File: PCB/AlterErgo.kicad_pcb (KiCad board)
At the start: 2 copper layers, 104 parts, among them J1 GS3, J2 SJ-43514, J3 GS3, J4 Conn_01x02, SW0:10 SW_Push, SW0:11 SW_Push, SW0:12 SW_Push, SW0:7 SW_Push, SW0:8 SW_Push, SW0:9 SW_Push, SW1 SW_SPST, SW1:10 SW_Push, SW1:11 SW_Push, SW1:12 SW_Push, SW1:13 SW_Push, SW1:7 SW_Push, SW1:8 SW_Push, SW1:9 SW_Push, SW2:10 SW_Push, SW2:11 SW_Push, SW2:12 SW_Push, SW2:13 SW_Push, SW2:7 SW_Push, SW2:8 SW_Push, SW2:9 SW_Push, SW3:10 SW_Push, SW3:11 SW_Push, SW3:12 SW_Push, SW3:13 SW_Push, SW3:8 SW_Push, SW3:9 SW_Push, SW4:10 SW_Push, SW4:11 SW_Push, SW4:12 SW_Push, SW4:13 SW_Push, SW4:7 SW_Push, SW4:8 SW_Push, SW4:9 SW_Push, SW5:10 SW_Push, SW5:11 SW_Push, SW5:12 SW_Push, SW5:13 SW_Push, SW5:7 SW_Push, SW5:8 SW_Push, SW5:9 SW_Push, U1 Feather32u4Bluefruit, U2 MCP23018

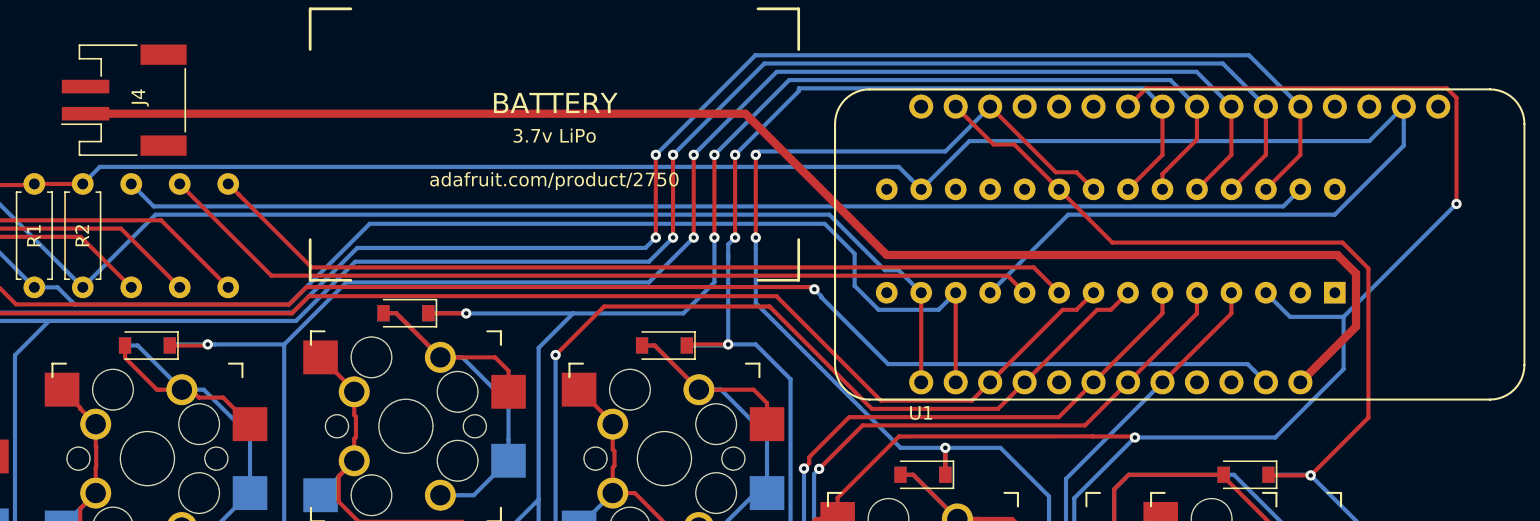
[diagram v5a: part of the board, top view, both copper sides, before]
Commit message: Fix some DRC errors
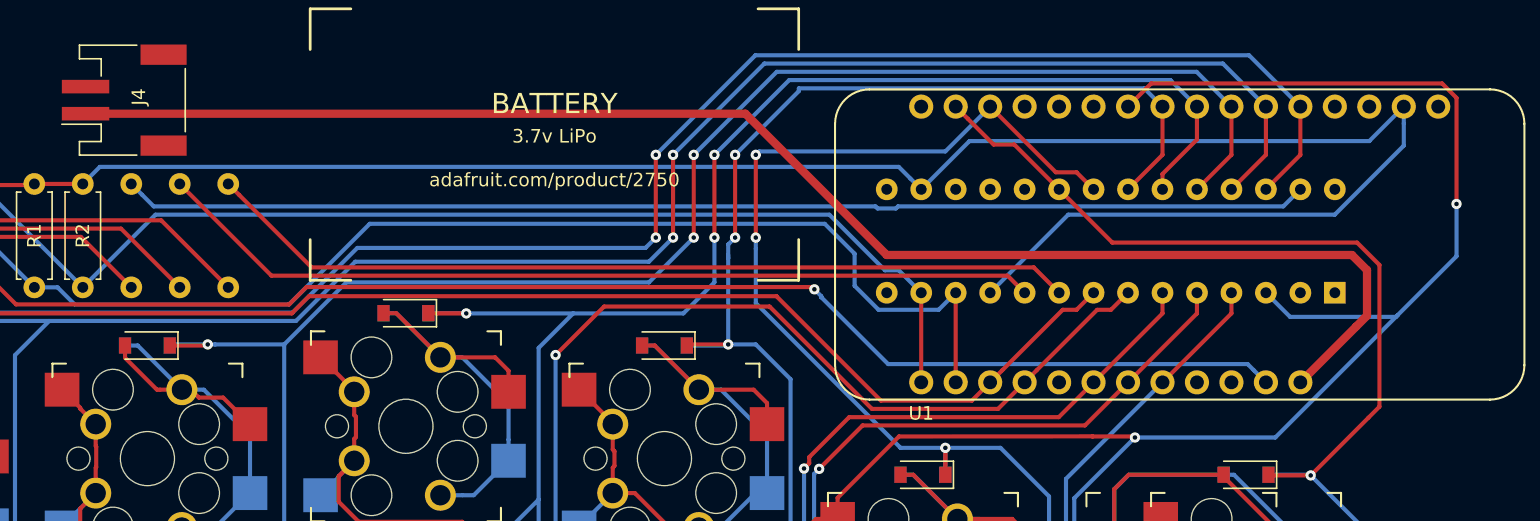
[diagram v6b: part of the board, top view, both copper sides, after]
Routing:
- net /ROW5: track 322.2 -> 326.5 mm
- net /COL0: track 193.5 -> 194.8 mm
- net Net-(J4-Pad1): track 108.2 -> 109.5 mm
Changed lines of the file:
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@@
     (thickness 1.6)
     (drawings 68)
-    (tracks 1733)
+    (tracks 1741)
     (zones 0)
     (modules 104)
@@
     (aux_axis_origin 0 0)
     (grid_origin 71.4375 47.625)
-    (visible_elements FFFFFF7F)
+    (visible_elements FFFFEF7F)
     (pcbplotparams
       (layerselection 0x00030_80000001)
@@
   (segment (start 174.5625 132.159375) (end 175.498125 132.159375) (width 0.3048) (layer F.Cu) (net 20))
   (segment (start 175.498125 132.159375) (end 178.7525 135.41375) (width 0.3048) (layer F.Cu) (net 20))
+  (segment (start 186.2455 34.925) (end 190.169869 38.849369) (width 0.3048) (layer F.Cu) (net 21))
+  (segment (start 208.20504 38.849369) (end 209.85191 40.496239) (width 0.3048) (layer F.Cu) (net 21))
+  (segment (start 209.85191 50.94259) (end 209.041911 51.752589) (width 0.3048) (layer F.Cu) (net 21))
+  (segment (start 190.169869 38.849369) (end 208.20504 38.849369) (width 0.3048) (layer F.Cu) (net 21))
+  (segment (start 209.85191 40.496239) (end 209.85191 50.94259) (width 0.3048) (layer F.Cu) (net 21))
+  (segment (start 209.041911 51.752589) (end 204.7875 56.007) (width 0.3048) (layer F.Cu) (net 21))
   (segment (start 209.317201 108.627299) (end 209.317201 127.677299) (width 0.3048) (layer B.Cu) (net 21))
   (segment (start 209.317201 127.677299) (end 204.7875 132.207) (width 0.3048) (layer B.Cu) (net 21))
@@
   (segment (start 209.6135 70.231) (end 204.7875 75.057) (width 0.3048) (layer B.Cu) (net 21))
   (segment (start 204.7875 56.007) (end 209.6135 60.833) (width 0.3048) (layer B.Cu) (net 21))
-  (segment (start 186.2455 34.925) (end 190.169869 38.849369) (width 0.3048) (layer F.Cu) (net 21))
-  (segment (start 190.169869 38.849369) (end 207.134642 38.849369) (width 0.3048) (layer F.Cu) (net 21))
-  (segment (start 207.134642 38.849369) (end 209.041911 40.756638) (width 0.3048) (layer F.Cu) (net 21))
-  (segment (start 209.041911 40.756638) (end 209.041911 51.752589) (width 0.3048) (layer F.Cu) (net 21))
-  (segment (start 209.041911 51.752589) (end 204.7875 56.007) (width 0.3048) (layer F.Cu) (net 21))
   (segment (start 204.7875 132.207) (end 196.960125 132.207) (width 0.3048) (layer F.Cu) (net 21))
   (segment (start 196.960125 132.207) (end 196.9125 132.159375) (width 0.3048) (layer F.Cu) (net 21))
@@
   (segment (start 182.448299 41.287799) (end 183.7055 42.545) (width 0.3048) (layer F.Cu) (net 58))
   (segment (start 121.44375 34.528125) (end 128.203424 41.287799) (width 0.3048) (layer F.Cu) (net 58))
+  (segment (start 202.768299 36.182201) (end 174.374509 36.182201) (width 0.3048) (layer B.Cu) (net 59))
+  (segment (start 174.374509 36.182201) (end 174.222109 36.334601) (width 0.3048) (layer B.Cu) (net 59))
+  (segment (start 174.222109 36.334601) (end 172.868891 36.334601) (width 0.3048) (layer B.Cu) (net 59))
+  (segment (start 172.868891 36.334601) (end 172.716491 36.182201) (width 0.3048) (layer B.Cu) (net 59))
+  (segment (start 172.716491 36.182201) (end 119.525951 36.182201) (width 0.3048) (layer B.Cu) (net 59))
   (segment (start 204.0255 34.925) (end 202.768299 36.182201) (width 0.3048) (layer B.Cu) (net 59))
-  (segment (start 202.768299 36.182201) (end 119.525951 36.182201) (width 0.3048) (layer B.Cu) (net 59))
   (segment (start 119.525951 36.182201) (end 118.671874 35.328124) (width 0.3048) (layer B.Cu) (net 59))
   (segment (start 118.671874 35.328124) (end 117.871875 34.528125) (width 0.3048) (layer B.Cu) (net 59))
@@
   (segment (start 198.9455 42.545) (end 198.9455 44.069) (width 0.3048) (layer F.Cu) (net 65))
   (segment (start 198.9455 44.069) (end 193.8655 49.149) (width 0.3048) (layer F.Cu) (net 65))
+  (segment (start 215.531701 36.001761) (end 215.531701 28.182823) (width 0.3048) (layer F.Cu) (net 66))
+  (segment (start 215.531701 28.182823) (end 214.473878 27.125) (width 0.3048) (layer F.Cu) (net 66))
+  (segment (start 214.473878 27.125) (end 193.0295 27.125) (width 0.3048) (layer F.Cu) (net 66))
+  (segment (start 193.0295 27.125) (end 192.671701 27.482799) (width 0.3048) (layer F.Cu) (net 66))
+  (segment (start 192.671701 27.482799) (end 191.3255 28.829) (width 0.3048) (layer F.Cu) (net 66))
+  (segment (start 215.531701 39.860729) (end 211.1875 44.20493) (width 0.3048) (layer B.Cu) (net 66))
+  (segment (start 211.1875 44.20493) (end 202.17943 53.213) (width 0.3048) (layer B.Cu) (net 66))
+  (segment (start 203.2635 44.323) (end 211.06943 44.323) (width 0.3048) (layer B.Cu) (net 66))
+  (segment (start 211.06943 44.323) (end 211.1875 44.20493) (width 0.3048) (layer B.Cu) (net 66))
+  (segment (start 215.531701 36.001761) (end 215.531701 39.860729) (width 0.3048) (layer B.Cu) (net 66))
+  (segment (start 202.17943 53.213) (end 191.8335 53.213) (width 0.3048) (layer B.Cu) (net 66))
   (segment (start 77.1525 54.61) (end 74.6725 52.13) (width 0.3048) (layer F.Cu) (net 66))
   (segment (start 74.6725 52.13) (end 74.6725 52.07) (width 0.3048) (layer F.Cu) (net 66))
@@
   (segment (start 191.8335 53.213) (end 187.36311 57.68339) (width 0.3048) (layer B.Cu) (net 66))
   (segment (start 187.36311 57.68339) (end 187.36311 67.28461) (width 0.3048) (layer B.Cu) (net 66))
-  (segment (start 191.8335 53.213) (end 202.17943 53.213) (width 0.3048) (layer B.Cu) (net 66))
-  (segment (start 202.17943 53.213) (end 207.210462 48.181968) (width 0.3048) (layer B.Cu) (net 66))
   (segment (start 188.709299 53.136799) (end 191.757299 53.136799) (width 0.3048) (layer F.Cu) (net 66))
   (via (at 191.8335 53.213) (size 0.762) (drill 0.3302) (layers F.Cu B.Cu) (net 66))
@@
   (segment (start 174.444651 53.136799) (end 169.9225 57.65895) (width 0.3048) (layer F.Cu) (net 66))
   (segment (start 169.9225 57.65895) (end 169.9225 59.21375) (width 0.3048) (layer F.Cu) (net 66))
-  (segment (start 207.210462 44.323) (end 207.210462 48.181968) (width 0.3048) (layer B.Cu) (net 66))
-  (segment (start 191.3255 28.829) (end 192.671701 27.482799) (width 0.3048) (layer F.Cu) (net 66))
-  (segment (start 192.671701 27.482799) (end 214.831677 27.482799) (width 0.3048) (layer F.Cu) (net 66))
-  (segment (start 214.831677 27.482799) (end 215.531701 28.182823) (width 0.3048) (layer F.Cu) (net 66))
-  (segment (start 215.531701 28.182823) (end 215.531701 36.001761) (width 0.3048) (layer F.Cu) (net 66))
   (via (at 215.531701 36.001761) (size 0.762) (drill 0.3302) (layers F.Cu B.Cu) (net 66))
   (segment (start 201.4855 42.545) (end 203.2635 44.323) (width 0.3048) (layer B.Cu) (net 66))
-  (segment (start 203.2635 44.323) (end 207.210462 44.323) (width 0.3048) (layer B.Cu) (net 66))
-  (segment (start 207.210462 44.323) (end 215.531701 36.001761) (width 0.3048) (layer B.Cu) (net 66))
-  (segment (start 163.1315 29.353125) (end 114.503125 29.353125) (width 0.6096) (layer F.Cu) (net 82))
-  (segment (start 204.0255 49.149) (end 208.127501 45.046999) (width 0.6096) (layer F.Cu) (net 82))
-  (segment (start 208.127501 45.046999) (end 208.127501 41.135399) (width 0.6096) (layer F.Cu) (net 82))
-  (segment (start 208.127501 41.135399) (end 206.755881 39.763779) (width 0.6096) (layer F.Cu) (net 82))
-  (segment (start 206.755881 39.763779) (end 173.542154 39.763779) (width 0.6096) (layer F.Cu) (net 82))
-  (segment (start 173.542154 39.763779) (end 163.1315 29.353125) (width 0.6096) (layer F.Cu) (net 82))
+  (segment (start 114.503125 29.353125) (end 163.1315 29.353125) (width 0.6096) (layer F.Cu) (net 82))
+  (segment (start 163.1315 29.353125) (end 173.542154 39.763779) (width 0.6096) (layer F.Cu) (net 82))
+  (segment (start 173.542154 39.763779) (end 207.826279 39.763779) (width 0.6096) (layer F.Cu) (net 82))
+  (segment (start 207.826279 39.763779) (end 208.9375 40.875) (width 0.6096) (layer F.Cu) (net 82))
+  (segment (start 208.9375 40.875) (end 208.9375 44.237) (width 0.6096) (layer F.Cu) (net 82))
+  (segment (start 208.9375 44.237) (end 208.127501 45.046999) (width 0.6096) (layer F.Cu) (net 82))
+  (segment (start 208.127501 45.046999) (end 204.0255 49.149) (width 0.6096) (layer F.Cu) (net 82))
 )
